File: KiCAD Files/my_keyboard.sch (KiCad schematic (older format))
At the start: 47 parts, among them K1 KEYSW, K10 KEYSW, K11 KEYSW, K12 KEYSW, K13 KEYSW, K14 KEYSW, K15 KEYSW, K16 KEYSW, K17 KEYSW, K2 KEYSW, K3 KEYSW, K4 KEYSW, K5 KEYSW, K6 KEYSW, K7 KEYSW, K8 KEYSW, K9 KEYSW, SW1 SW_Push, SW2 Rotary_Encoder_Switch, SW3 Rotary_Encoder_Switch, SW4 Rotary_Encoder_Switch

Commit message: Update PCB
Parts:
- D1, D10, D11, D12, D13, D14, D15, D16, D17, D18, D19, D2, D20, D3, D4, D5, D6, D7, D8, D9: footprint Diode_THT:D_DO-35_SOD27_P10.16mm_Horizontal -> keyboard_parts:D_SOD123_axial
- H1, H2, H3, H4: footprint (none) -> MountingHole:MountingHole_4.3mm_M4_Pad_Via
- SW1: footprint Button_Switch_THT:SW_PUSH_6mm -> Button_Switch_SMD:SW_PUSH_4_5.1x5.1mm
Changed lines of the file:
@@
 F 0 "D1" V 6954 1628 50  0000 L CNN
 F 1 "DIODE" V 7045 1628 50  0000 L CNN
-F 2 "Diode_THT:D_DO-35_SOD27_P10.16mm_Horizontal" H 7000 1500 50  0001 C CNN
+F 2 "keyboard_parts:D_SOD123_axial" H 7000 1500 50  0001 C CNN
 F 3 "~" H 7000 1500 50  0001 C CNN
 	1    7000 1500
@@
 F 0 "D2" V 6954 2478 50  0000 L CNN
 F 1 "DIODE" V 7045 2478 50  0000 L CNN
-F 2 "Diode_THT:D_DO-35_SOD27_P10.16mm_Horizontal" H 7000 2350 50  0001 C CNN
+F 2 "keyboard_parts:D_SOD123_axial" H 7000 2350 50  0001 C CNN
 F 3 "~" H 7000 2350 50  0001 C CNN
 	1    7000 2350
@@
 F 0 "D3" V 6954 3328 50  0000 L CNN
 F 1 "DIODE" V 7045 3328 50  0000 L CNN
-F 2 "Diode_THT:D_DO-35_SOD27_P10.16mm_Horizontal" H 7000 3200 50  0001 C CNN
+F 2 "keyboard_parts:D_SOD123_axial" H 7000 3200 50  0001 C CNN
 F 3 "~" H 7000 3200 50  0001 C CNN
 	1    7000 3200
@@
 F 0 "D4" V 6954 4178 50  0000 L CNN
 F 1 "DIODE" V 7045 4178 50  0000 L CNN
-F 2 "Diode_THT:D_DO-35_SOD27_P10.16mm_Horizontal" H 7000 4050 50  0001 C CNN
+F 2 "keyboard_parts:D_SOD123_axial" H 7000 4050 50  0001 C CNN
 F 3 "~" H 7000 4050 50  0001 C CNN
 	1    7000 4050
@@
 F 0 "D5" V 6954 5028 50  0000 L CNN
 F 1 "DIODE" V 7045 5028 50  0000 L CNN
-F 2 "Diode_THT:D_DO-35_SOD27_P10.16mm_Horizontal" H 7000 4900 50  0001 C CNN
+F 2 "keyboard_parts:D_SOD123_axial" H 7000 4900 50  0001 C CNN
 F 3 "~" H 7000 4900 50  0001 C CNN
 	1    7000 4900
@@
 F 0 "D6" V 7954 1628 50  0000 L CNN
 F 1 "DIODE" V 8045 1628 50  0000 L CNN
-F 2 "Diode_THT:D_DO-35_SOD27_P10.16mm_Horizontal" H 8000 1500 50  0001 C CNN
+F 2 "keyboard_parts:D_SOD123_axial" H 8000 1500 50  0001 C CNN
 F 3 "~" H 8000 1500 50  0001 C CNN
 	1    8000 1500
@@
 F 0 "D7" V 7954 2478 50  0000 L CNN
 F 1 "DIODE" V 8045 2478 50  0000 L CNN
-F 2 "Diode_THT:D_DO-35_SOD27_P10.16mm_Horizontal" H 8000 2350 50  0001 C CNN
+F 2 "keyboard_parts:D_SOD123_axial" H 8000 2350 50  0001 C CNN
 F 3 "~" H 8000 2350 50  0001 C CNN
 	1    8000 2350
@@
 F 0 "D8" V 7954 3328 50  0000 L CNN
 F 1 "DIODE" V 8045 3328 50  0000 L CNN
-F 2 "Diode_THT:D_DO-35_SOD27_P10.16mm_Horizontal" H 8000 3200 50  0001 C CNN
+F 2 "keyboard_parts:D_SOD123_axial" H 8000 3200 50  0001 C CNN
 F 3 "~" H 8000 3200 50  0001 C CNN
 	1    8000 3200
@@
 F 0 "D9" V 7954 4178 50  0000 L CNN
 F 1 "DIODE" V 8045 4178 50  0000 L CNN
-F 2 "Diode_THT:D_DO-35_SOD27_P10.16mm_Horizontal" H 8000 4050 50  0001 C CNN
+F 2 "keyboard_parts:D_SOD123_axial" H 8000 4050 50  0001 C CNN
 F 3 "~" H 8000 4050 50  0001 C CNN
 	1    8000 4050
@@
 F 0 "D10" V 7954 5028 50  0000 L CNN
 F 1 "DIODE" V 8045 5028 50  0000 L CNN
-F 2 "Diode_THT:D_DO-35_SOD27_P10.16mm_Horizontal" H 8000 4900 50  0001 C CNN
+F 2 "keyboard_parts:D_SOD123_axial" H 8000 4900 50  0001 C CNN
 F 3 "~" H 8000 4900 50  0001 C CNN
 	1    8000 4900
@@
 F 0 "D11" V 8954 1628 50  0000 L CNN
 F 1 "DIODE" V 9045 1628 50  0000 L CNN
-F 2 "Diode_THT:D_DO-35_SOD27_P10.16mm_Horizontal" H 9000 1500 50  0001 C CNN
+F 2 "keyboard_parts:D_SOD123_axial" H 9000 1500 50  0001 C CNN
 F 3 "~" H 9000 1500 50  0001 C CNN
 	1    9000 1500
@@
 F 0 "D12" V 8954 2478 50  0000 L CNN
 F 1 "DIODE" V 9045 2478 50  0000 L CNN
-F 2 "Diode_THT:D_DO-35_SOD27_P10.16mm_Horizontal" H 9000 2350 50  0001 C CNN
+F 2 "keyboard_parts:D_SOD123_axial" H 9000 2350 50  0001 C CNN
 F 3 "~" H 9000 2350 50  0001 C CNN
 	1    9000 2350
@@
 F 0 "D13" V 8954 3328 50  0000 L CNN
 F 1 "DIODE" V 9045 3328 50  0000 L CNN
-F 2 "Diode_THT:D_DO-35_SOD27_P10.16mm_Horizontal" H 9000 3200 50  0001 C CNN
+F 2 "keyboard_parts:D_SOD123_axial" H 9000 3200 50  0001 C CNN
 F 3 "~" H 9000 3200 50  0001 C CNN
 	1    9000 3200
@@
 F 0 "D14" V 8954 4178 50  0000 L CNN
 F 1 "DIODE" V 9045 4178 50  0000 L CNN
-F 2 "Diode_THT:D_DO-35_SOD27_P10.16mm_Horizontal" H 9000 4050 50  0001 C CNN
+F 2 "keyboard_parts:D_SOD123_axial" H 9000 4050 50  0001 C CNN
 F 3 "~" H 9000 4050 50  0001 C CNN
 	1    9000 4050
@@
 F 0 "D18" V 9954 3328 50  0000 L CNN
 F 1 "DIODE" V 10045 3328 50  0000 L CNN
-F 2 "Diode_THT:D_DO-35_SOD27_P10.16mm_Horizontal" H 10000 3200 50  0001 C CNN
+F 2 "keyboard_parts:D_SOD123_axial" H 10000 3200 50  0001 C CNN
 F 3 "~" H 10000 3200 50  0001 C CNN
 	1    10000 3200
@@
 F 0 "D16" V 9954 1628 50  0000 L CNN
 F 1 "DIODE" V 10045 1628 50  0000 L CNN
-F 2 "Diode_THT:D_DO-35_SOD27_P10.16mm_Horizontal" H 10000 1500 50  0001 C CNN
+F 2 "keyboard_parts:D_SOD123_axial" H 10000 1500 50  0001 C CNN
 F 3 "~" H 10000 1500 50  0001 C CNN
 	1    10000 1500
@@
 F 0 "D17" V 9954 2478 50  0000 L CNN
 F 1 "DIODE" V 10045 2478 50  0000 L CNN
-F 2 "Diode_THT:D_DO-35_SOD27_P10.16mm_Horizontal" H 10000 2350 50  0001 C CNN
+F 2 "keyboard_parts:D_SOD123_axial" H 10000 2350 50  0001 C CNN
 F 3 "~" H 10000 2350 50  0001 C CNN
 	1    10000 2350
@@
 F 0 "D19" V 9954 4178 50  0000 L CNN
 F 1 "DIODE" V 10045 4178 50  0000 L CNN
-F 2 "Diode_THT:D_DO-35_SOD27_P10.16mm_Horizontal" H 10000 4050 50  0001 C CNN
+F 2 "keyboard_parts:D_SOD123_axial" H 10000 4050 50  0001 C CNN
 F 3 "~" H 10000 4050 50  0001 C CNN
 	1    10000 4050
@@
 F 0 "SW1" H 1300 6835 50  0000 C CNN
 F 1 "SW_Push" H 1300 6744 50  0000 C CNN
-F 2 "Button_Switch_THT:SW_PUSH_6mm" H 1300 6750 50  0001 C CNN
+F 2 "Button_Switch_SMD:SW_PUSH_4_5.1x5.1mm" H 1300 6750 50  0001 C CNN
 F 3 "~" H 1300 6750 50  0001 C CNN
 	1    1300 6550
@@
 F 0 "D15" V 8954 5028 50  0000 L CNN
 F 1 "DIODE" V 9045 5028 50  0000 L CNN
-F 2 "Diode_THT:D_DO-35_SOD27_P10.16mm_Horizontal" H 9000 4900 50  0001 C CNN
+F 2 "keyboard_parts:D_SOD123_axial" H 9000 4900 50  0001 C CNN
 F 3 "~" H 9000 4900 50  0001 C CNN
 	1    9000 4900
@@
 F 0 "D20" V 9954 5028 50  0000 L CNN
 F 1 "DIODE" V 10045 5028 50  0000 L CNN
-F 2 "Diode_THT:D_DO-35_SOD27_P10.16mm_Horizontal" H 10000 4900 50  0001 C CNN
+F 2 "keyboard_parts:D_SOD123_axial" H 10000 4900 50  0001 C CNN
 F 3 "~" H 10000 4900 50  0001 C CNN
 	1    10000 4900
@@
 F 0 "H1" V 4604 4150 50  0000 L CNN
 F 1 "MountingHole_Pad" V 4695 4150 50  0000 L CNN
-F 2 "" H 4650 4000 50  0001 C CNN
+F 2 "MountingHole:MountingHole_4.3mm_M4_Pad_Via" H 4650 4000 50  0001 C CNN
 F 3 "~" H 4650 4000 50  0001 C CNN
 	1    4650 4000
@@
 F 0 "H2" V 4604 4450 50  0000 L CNN
 F 1 "MountingHole_Pad" V 4695 4450 50  0000 L CNN
-F 2 "" H 4650 4300 50  0001 C CNN
+F 2 "MountingHole:MountingHole_4.3mm_M4_Pad_Via" H 4650 4300 50  0001 C CNN
 F 3 "~" H 4650 4300 50  0001 C CNN
 	1    4650 4300
@@
 F 0 "H3" V 4604 4750 50  0000 L CNN
 F 1 "MountingHole_Pad" V 4695 4750 50  0000 L CNN
-F 2 "" H 4650 4600 50  0001 C CNN
+F 2 "MountingHole:MountingHole_4.3mm_M4_Pad_Via" H 4650 4600 50  0001 C CNN
 F 3 "~" H 4650 4600 50  0001 C CNN
 	1    4650 4600
@@
 F 0 "H4" V 4604 5050 50  0000 L CNN
 F 1 "MountingHole_Pad" V 4695 5050 50  0000 L CNN
-F 2 "" H 4650 4900 50  0001 C CNN
+F 2 "MountingHole:MountingHole_4.3mm_M4_Pad_Via" H 4650 4900 50  0001 C CNN
 F 3 "~" H 4650 4900 50  0001 C CNN
 	1    4650 4900

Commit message: Updated KiCAD Schem
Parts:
- added C1, C2, C3, C6: 0.1uF, symbol Device:C_Small
- added C4, C5: 22pF, symbol Device:C_Small
- added C7: 1uF, symbol Device:C_Small
- added F?: 500 mA, symbol Device:Polyfuse_Small
- added J?: USB_B_Mini, symbol Connector:USB_B_Mini
- added R1, R2: 22, symbol Device:R
- added R3, R4: 10k, symbol Device:R
- added U1: ATmega32U4-AU, Package_QFP:TQFP-44_10x10mm_P0.8mm, symbol MCU_Microchip_ATmega:ATmega32U4-AU
- added Y1: 16MHz, symbol Device:Crystal_GND24_Small
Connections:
- net GND: now also SW1.1, C1.2, C2.2, C3.2, C4.2, C5.2, C6.2, C7.2, J?.5 (GND), J?.6 (Shield), R4.1, Y1.2, Y1.4; no longer SW1.2
- net RESET_SW: no longer SW1.1
- net VCC: now also F?.2, J?.1 (VBUS)
- new net: R3.2, SW1.2, U1.13 (~RESET)
- new net: U1.15 (GND), U1.23 (GND), U1.35 (GND), U1.43 (GND), U1.5 (UGND)
- new net: C5.1, U1.16 (XTAL2), Y1.3
- new net: C4.1, U1.17 (XTAL1), Y1.1
- new net: R2.1, U1.3 (D-)
- new net: R4.2, U1.33 (~HWB~/PE2)
- new net: R1.1, U1.4 (D+)
- new net: C7.1, U1.6 (UCAP)
- new net +5V: C1.1, C2.1, C3.1, C6.1, F?.1, R3.1, U1.14 (VCC), U1.2 (UVCC), U1.24 (AVCC), U1.34 (VCC), U1.44 (AVCC), U1.7 (VBUS)
- new net D+: J?.3 (D+), R1.2
- new net D-: J?.2 (D-), R2.2
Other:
- moved on the sheet: B1, DS1, H1, H2, H3, H4, SW1, SW2, SW3, SW4

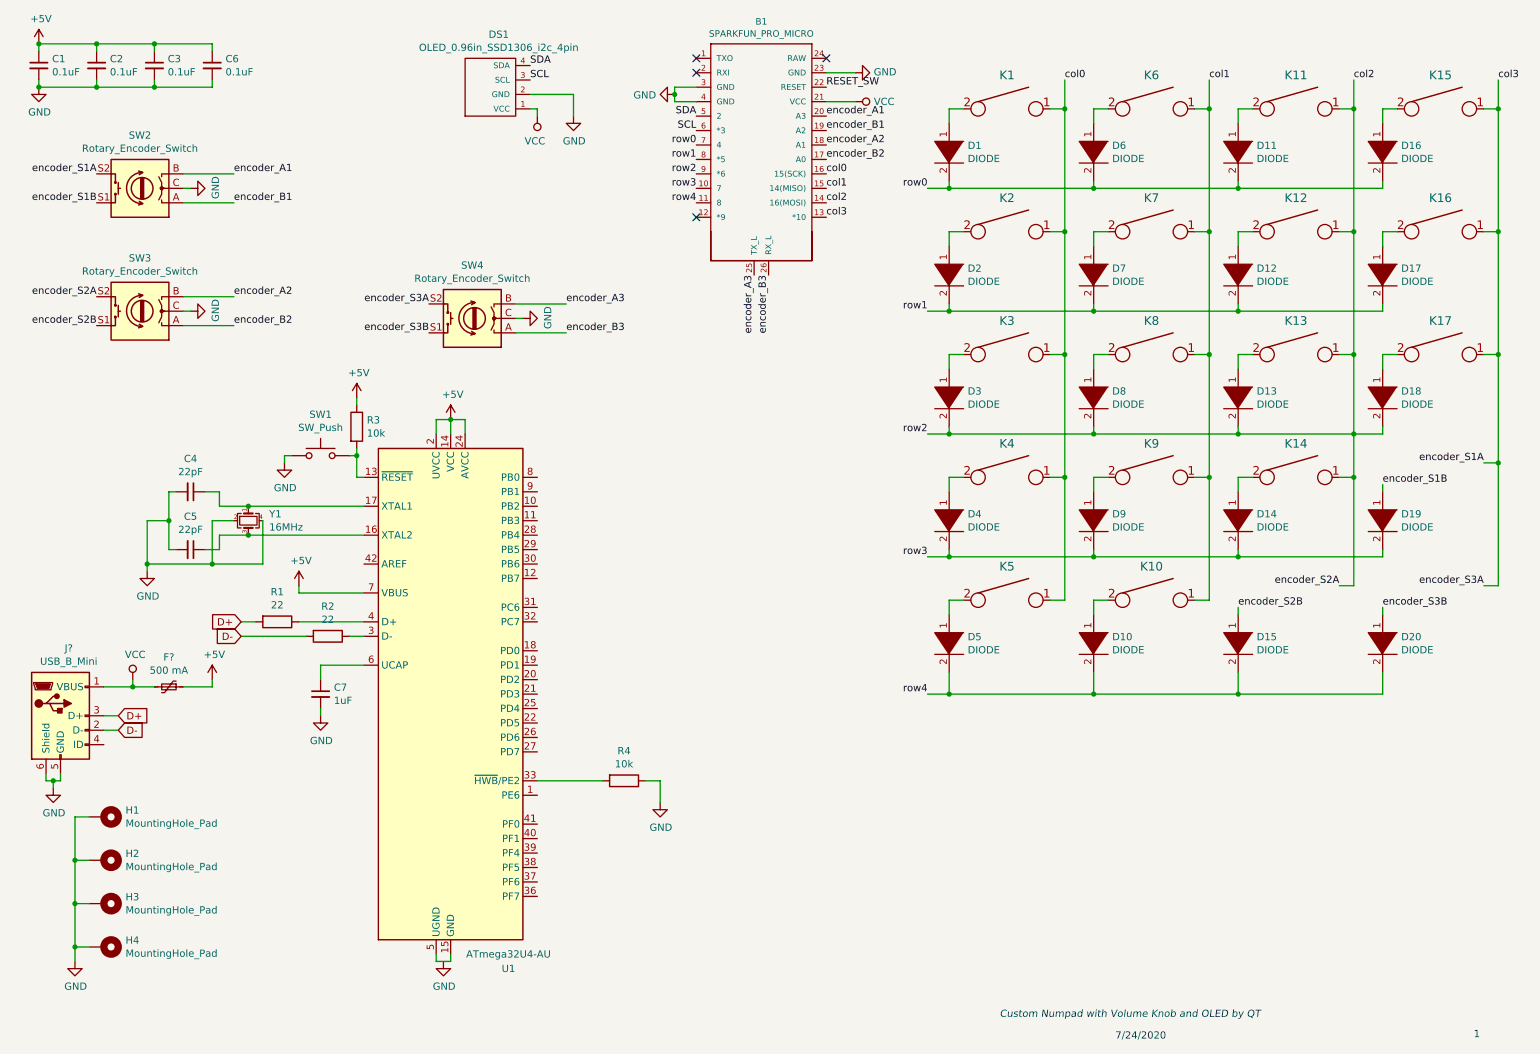
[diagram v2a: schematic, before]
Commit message: Fixed Diode Issue
Previously used wrong diode symbol meant for simulation not design.
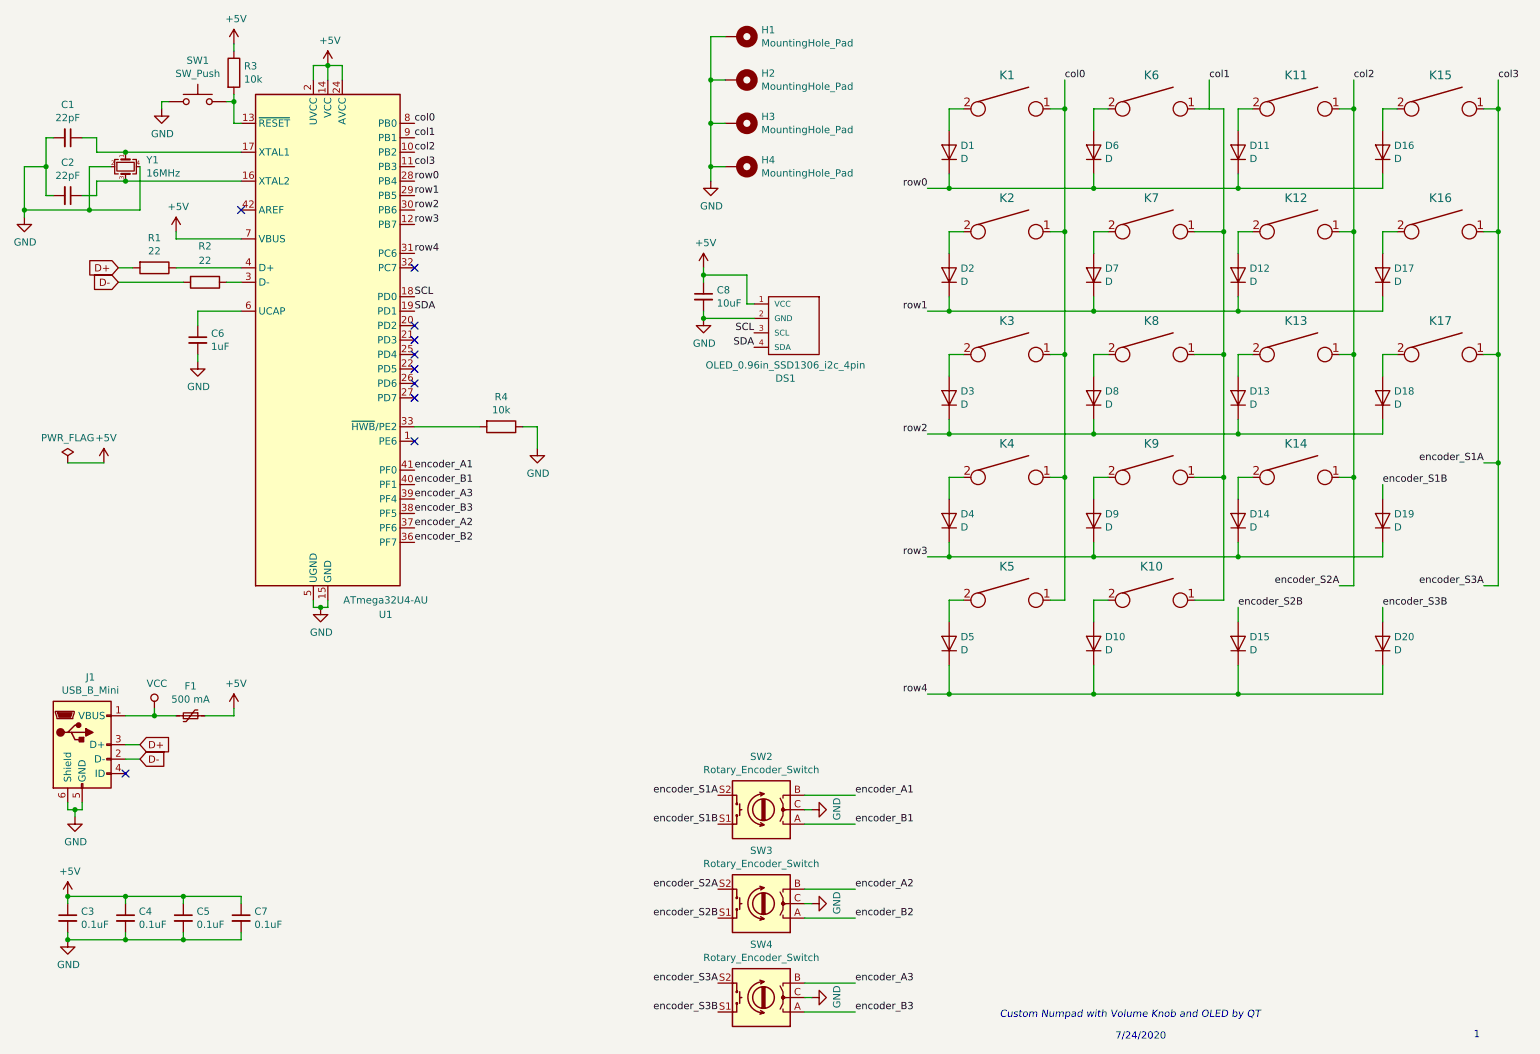
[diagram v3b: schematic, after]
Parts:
- removed B1: SPARKFUN_PRO_MICRO, SparkFun:SPARKFUN_PRO_MICRO, symbol SparkFun-Boards:SPARKFUN_PRO_MICRO
- removed D1, D10, D11, D12, D13, D14, D15, D16, D17, D18, D19, D2, D20, D3, D4, D5, D6, D7, D8, D9: DIODE, keyboard_parts:D_SOD123_axial, symbol pspice:DIODE
- added C8: 10uF, Capacitor_SMD:C_0805_2012Metric_Pad1.15x1.40mm_HandSolder, symbol Device:C_Small
- added D1, D10, D11, D12, D13, D14, D15, D16, D17, D18, D19, D2, D20, D3, D4, D5, D6, D7, D8, D9: D, Diode_SMD:D_SOD-123, symbol Device:D
- C1: renamed from C4; footprint (none) -> Capacitor_SMD:C_0805_2012Metric_Pad1.15x1.40mm_HandSolder
- C2: renamed from C5; footprint (none) -> Capacitor_SMD:C_0805_2012Metric_Pad1.15x1.40mm_HandSolder
- C3: renamed from C1; footprint (none) -> Capacitor_SMD:C_0805_2012Metric_Pad1.15x1.40mm_HandSolder
- C4: renamed from C2; footprint (none) -> Capacitor_SMD:C_0805_2012Metric_Pad1.15x1.40mm_HandSolder
- C5: renamed from C3; footprint (none) -> Capacitor_SMD:C_0805_2012Metric_Pad1.15x1.40mm_HandSolder
- C6: renamed from C7; footprint (none) -> Capacitor_SMD:C_0805_2012Metric_Pad1.15x1.40mm_HandSolder
- C7: renamed from C6; footprint (none) -> Capacitor_SMD:C_0805_2012Metric_Pad1.15x1.40mm_HandSolder
- F1: renamed from F?; footprint (none) -> Fuse:Fuse_1206_3216Metric_Pad1.42x1.75mm_HandSolder
- H1, H2, H3, H4: footprint MountingHole:MountingHole_4.3mm_M4_Pad_Via -> MountingHole:MountingHole_3.2mm_M3_Pad_Via
- J1: renamed from J?; footprint (none) -> random-keyboard-parts:Molex-0548190589
- K16, K17: footprint Button_Switch_Keyboard:SW_Cherry_MX_1.00u_PCB -> Button_Switch_Keyboard:SW_Cherry_MX_2.00u_Vertical_Plate
- K5: footprint Button_Switch_Keyboard:SW_Cherry_MX_1.00u_PCB -> Button_Switch_Keyboard:SW_Cherry_MX_2.00u_Plate
- R1, R2, R3, R4: footprint (none) -> Resistor_SMD:R_0805_2012Metric_Pad1.15x1.40mm_HandSolder
- Y1: footprint (none) -> Crystal:Crystal_SMD_3225-4Pin_3.2x2.5mm_HandSoldering
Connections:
- net +5V: now also DS1.1 (VCC), C8.1
- net GND: now also U1.15 (GND), U1.23 (GND), U1.35 (GND), U1.43 (GND), U1.5 (UGND), C8.2
- net SCL: now also U1.18 (PD0)
- net SDA: now also U1.19 (PD1)
- net VCC: no longer DS1.1 (VCC)
- net col0: now also U1.8 (PB0)
- net col1: now also U1.9 (PB1)
- net col2: now also U1.10 (PB2)
- net col3: now also U1.11 (PB3)
- net encoder_A1: now also U1.41 (PF0)
- net encoder_A2: now also U1.37 (PF6)
- net encoder_A3: now also U1.39 (PF4)
- net encoder_B1: now also U1.40 (PF1)
- net encoder_B2: now also U1.36 (PF7)
- net encoder_B3: now also U1.38 (PF5)
- net encoder_S1B: now also D19.2 (A)
- net encoder_S2B: now also D15.2 (A)
- net encoder_S3B: now also D20.2 (A)
- net row0: now also U1.28 (PB4), D1.1 (K), D11.1 (K), D16.1 (K), D6.1 (K)
- net row1: now also U1.29 (PB5), D12.1 (K), D17.1 (K), D2.1 (K), D7.1 (K)
- net row3: now also U1.12 (PB7), D14.1 (K), D19.1 (K), D4.1 (K), D9.1 (K)
- net row4: now also U1.31 (PC6), D10.1 (K), D15.1 (K), D20.1 (K), D5.1 (K)
- net at K1.2: now also D1.2 (A)
- net at K2.2: now also D2.2 (A)
- net at K3.2: now also D3.2 (A)
- net at K4.2: now also D4.2 (A)
- net at K5.2: now also D5.2 (A)
- net at K6.2: now also D6.2 (A)
- net at K7.2: now also D7.2 (A)
- net at K8.2: now also D8.2 (A)
- net at K9.2: now also D9.2 (A)
- net at K10.2: now also D10.2 (A)
- net at K11.2: now also D11.2 (A)
- net at K12.2: now also D12.2 (A)
- net at K13.2: now also D13.2 (A)
- net at K14.2: now also D14.2 (A)
- net at K17.2: now also D18.2 (A)
- net at K15.2: now also D16.2 (A)
- net at K16.2: now also D17.2 (A)
- net row2: now reaches U1.30 (PB6)
- net row2: now also D13.1 (K), D18.1 (K), D3.1 (K), D8.1 (K)
- no-connect marks 4 -> 10
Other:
- moved on the sheet: C1, C2, C3, C4, C5, C6, C7, DS1, F1, H1, H2, H3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
